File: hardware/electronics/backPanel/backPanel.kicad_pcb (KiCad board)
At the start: 2 copper layers, 104 x 54.6 mm, 8 parts, among them J1 Untitled, J2 Untitled, J3 Untitled, J4 7793, J5 M3, J6 M3, J7 M3, J8 M3

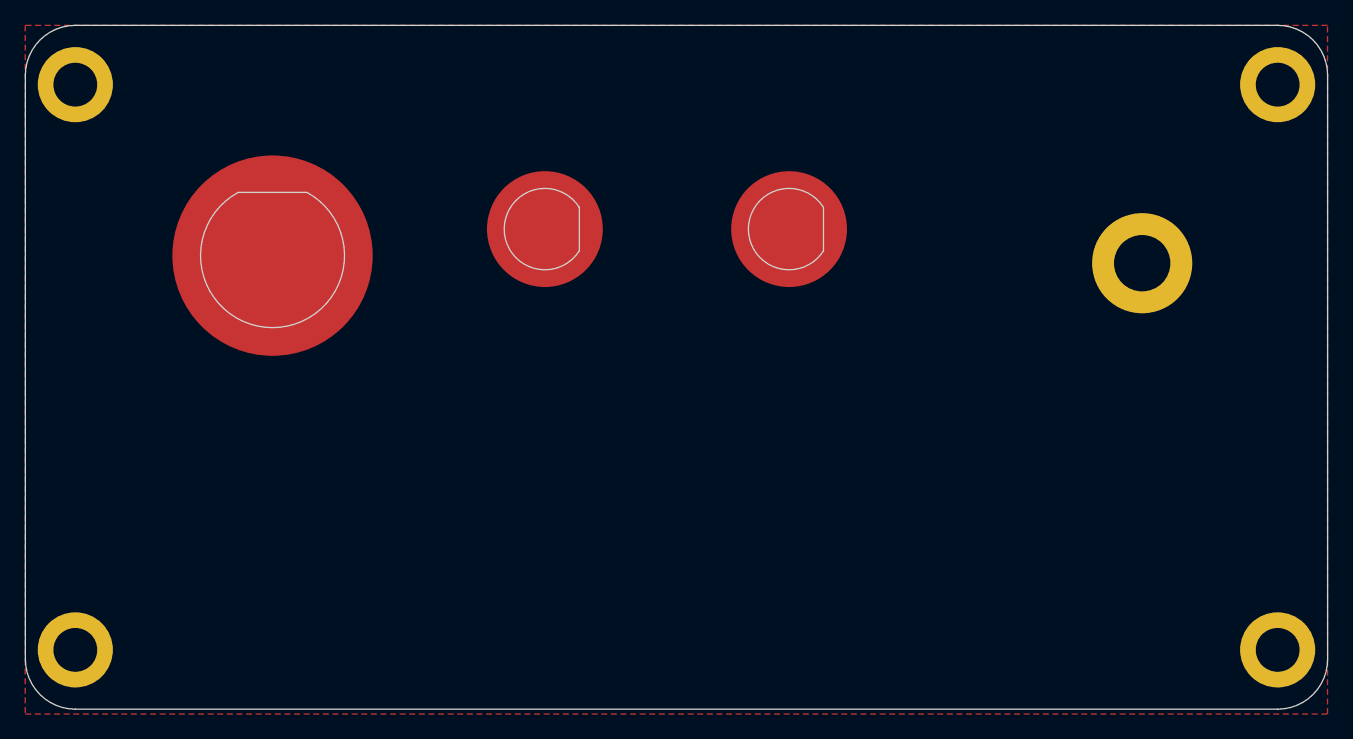
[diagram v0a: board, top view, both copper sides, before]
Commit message: front/back enclosure panels
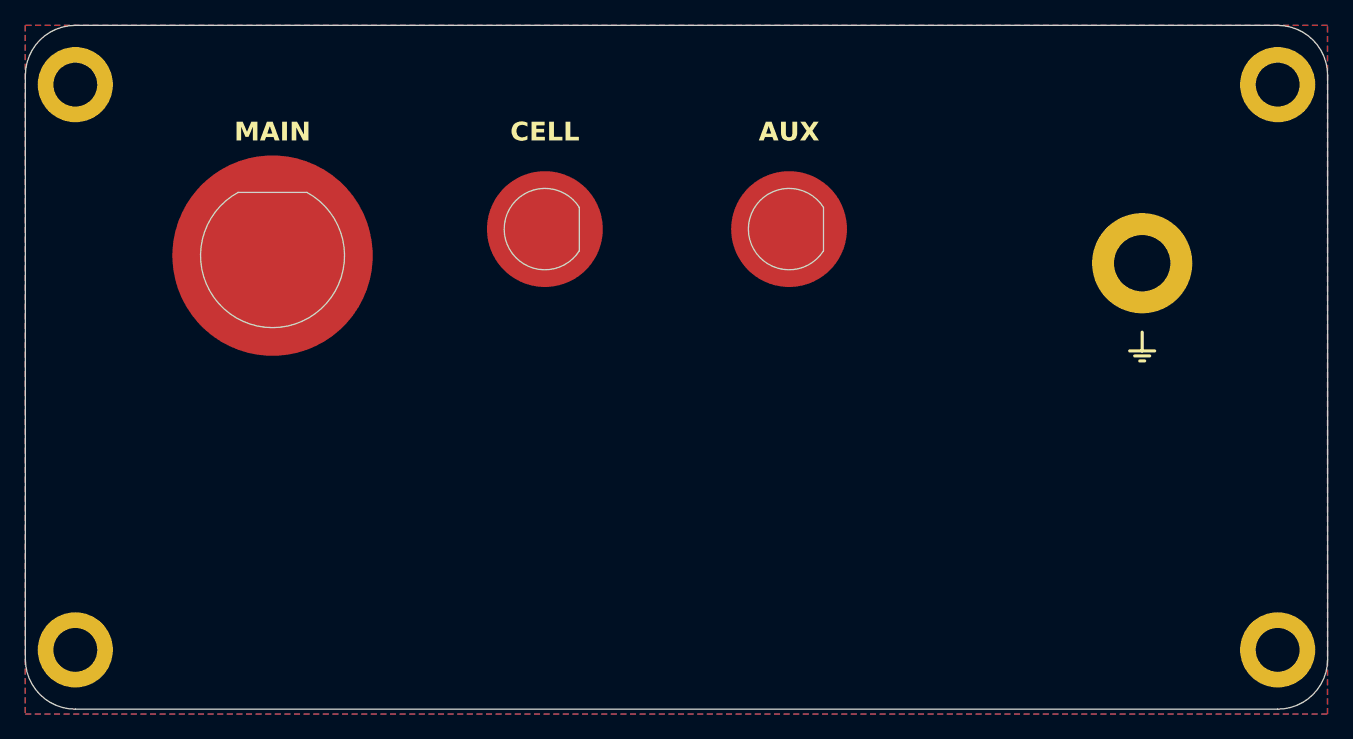
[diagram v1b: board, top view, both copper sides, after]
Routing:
- added copper zone on B.Cu, net GND
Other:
- board text added: "AUX"
- board text added: "CELL"
- board text added: "MAIN"
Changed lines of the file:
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@@
 		(embedded_fonts no)
+	)
+	(gr_line
+		(start 179 106.8)
+		(end 179.4 106.8)
+		(stroke
+			(width 0.25)
+			(type solid)
+		)
+		(layer "F.SilkS")
+	)
+	(gr_line
+		(start 178.6 106.4)
+		(end 179.8 106.4)
+		(stroke
+			(width 0.25)
+			(type solid)
+		)
+		(layer "F.SilkS")
+	)
+	(gr_line
+		(start 179.2 104.5)
+		(end 179.2 106)
+		(stroke
+			(width 0.25)
+			(type solid)
+		)
+		(layer "F.SilkS")
+	)
+	(gr_line
+		(start 178.2 106)
+		(end 180.2 106)
+		(stroke
+			(width 0.25)
+			(type solid)
+		)
+		(layer "F.SilkS")
 	)
 	(gr_arc
@@
 		)
 		(layer "Edge.Cuts")
+	)
+	(gr_text "AUX"
+		(at 151 88.5 0)
+		(layer "F.SilkS")
+		(effects
+			(font
+				(face "Arial")
+				(size 1.5 1.5)
+				(thickness 0.3)
+				(bold yes)
+			)
+		)
+		(render_cache "AUX" 0
+			(polygon
+				(pts
+					(xy 150.292276 89.1225) (xy 149.962273 89.1225) (xy 149.831115 88.782513) (xy 149.230735 88.782513)
+					(xy 149.106721 89.1225) (xy 148.784962 89.1225) (xy 149.014897 88.530455) (xy 149.323975 88.530455)
+					(xy 149.733845 88.530455) (xy 149.526849 87.967719) (xy 149.323975 88.530455) (xy 149.014897 88.530455)
+					(xy 149.370045 87.61601) (xy 149.690797 87.61601)
+				)
+			)
+			(polygon
+				(pts
+					(xy 150.450911 87.61601) (xy 150.754169 87.61601) (xy 150.754169 88.439322) (xy 150.757853 88.618371)
+					(xy 150.765435 88.693395) (xy 150.78465 88.752054) (xy 150.815323 88.8015) (xy 150.858125 88.843238)
+					(xy 150.909884 88.873342) (xy 150.975473 88.892706) (xy 151.058527 88.89975) (xy 151.143145 88.892843)
+					(xy 151.206385 88.874333) (xy 151.253158 88.846352) (xy 151.291596 88.807367) (xy 151.317496 88.764002)
+					(xy 151.332018 88.715194) (xy 151.341336 88.624569) (xy 151.34539 88.456999) (xy 151.34539 87.61601)
+					(xy 151.648739 87.61601) (xy 151.648739 88.409188) (xy 151.6412 88.661199) (xy 151.624101 88.793413)
+					(xy 151.602544 88.865826) (xy 151.57227 88.928557) (xy 151.533426 88.982915) (xy 151.485805 89.029773)
+					(xy 151.427398 89.070827) (xy 151.356655 89.106013) (xy 151.281421 89.130039) (xy 151.186481 89.145966)
+					(xy 151.067777 89.151809) (xy 150.923632 89.145067) (xy 150.81753 89.127375) (xy 150.741347 89.101892)
+					(xy 150.670502 89.064018) (xy 150.612479 89.020745) (xy 150.565675 88.972107) (xy 150.51142 88.888938)
+					(xy 150.480587 88.804678) (xy 150.459594 88.659457) (xy 150.450911 88.421461)
+				)
+			)
+			(polygon
+				(pts
+					(xy 151.815527 89.1225) (xy 152.335214 88.338846) (xy 151.863704 87.61601) (xy 152.218253 87.61601)
+					(xy 152.515649 88.066821) (xy 152.814602 87.61601) (xy 153.166037 87.61601) (xy 152.693885 88.336923)
+					(xy 153.212199 89.1225) (xy 152.846384 89.1225) (xy 152.513542 88.612246) (xy 152.179326 89.1225)
+				)
+			)
+		)
+	)
+	(gr_text "CELL"
+		(at 131.5 88.5 0)
+		(layer "F.SilkS")
+		(effects
+			(font
+				(face "Arial")
+				(size 1.5 1.5)
+				(thickness 0.3)
+				(bold yes)
+			)
+		)
+		(render_cache "CELL" 0
+			(polygon
+				(pts
+					(xy 129.874166 88.565626) (xy 130.168265 88.659415) (xy 130.126303 88.780938) (xy 130.074475 88.880565)
+					(xy 130.013496 88.961486) (xy 129.943318 89.026146) (xy 129.862223 89.077128) (xy 129.77004 89.114436)
+					(xy 129.66484 89.137768) (xy 129.544255 89.145947) (xy 129.425899 89.137333) (xy 129.319213 89.11237)
+					(xy 129.222314 89.071717) (xy 129.133699 89.015137) (xy 129.05232 88.941516) (xy 128.985229 88.85714)
+					(xy 128.932168 88.760992) (xy 128.89299 88.651371) (xy 128.868356 88.526083) (xy 128.859704 88.382535)
+					(xy 128.868561 88.229799) (xy 128.893638 88.097936) (xy 128.933248 87.983969) (xy 128.986496 87.88536)
+					(xy 129.053327 87.800108) (xy 129.13497 87.72594) (xy 129.225262 87.668592) (xy 129.325419 87.627108)
+					(xy 129.43717 87.601463) (xy 129.562665 87.592562) (xy 129.698743 87.603536) (xy 129.816755 87.634897)
+					(xy 129.919864 87.685437) (xy 130.010454 87.755503) (xy 130.07043 87.825247) (xy 130.121927 87.916044)
+					(xy 130.164144 88.032199) (xy 129.863908 88.102541) (xy 129.839054 88.028735) (xy 129.802082 87.967975)
+					(xy 129.752717 87.918169) (xy 129.693242 87.880999) (xy 129.625488 87.85835) (xy 129.547278 87.850483)
+					(xy 129.466077 87.858322) (xy 129.395094 87.880938) (xy 129.332253 87.918036) (xy 129.276168 87.970742)
+					(xy 129.234517 88.032613) (xy 129.202001 88.114586) (xy 129.180272 88.221698) (xy 129.172213 88.360004)
+					(xy 129.180333 88.507757) (xy 129.20204 88.620308) (xy 129.234143 88.704703) (xy 129.274703 88.766851)
+					(xy 129.330121 88.820121) (xy 129.391989 88.857473) (xy 129.461648 88.880173) (xy 129.541141 88.888026)
+					(xy 129.618776 88.879198) (xy 129.687386 88.853432) (xy 129.749145 88.810266) (xy 129.798761 88.752992)
+					(xy 129.840843 88.673372)
+				)
+			)
+			(polygon
+				(pts
+					(xy 130.428292 89.1225) (xy 130.428292 87.61601) (xy 131.542131 87.61601) (xy 131.542131 87.868068)
+					(xy 130.73155 87.868068) (xy 130.73155 88.202192) (xy 131.485711 88.202192) (xy 131.485711 88.454251)
+					(xy 130.73155 88.454251) (xy 130.73155 88.870441) (xy 131.570799 88.870441) (xy 131.570799 89.1225)
+				)
+			)
+			(polygon
+				(pts
+					(xy 131.835956 89.1225) (xy 131.835956 87.633595) (xy 132.139305 87.633595) (xy 132.139305 88.870441)
+					(xy 132.893466 88.870441) (xy 132.893466 89.1225)
+				)
+			)
+			(polygon
+				(pts
+					(xy 133.118231 89.1225) (xy 133.118231 87.633595) (xy 133.42158 87.633595) (xy 133.42158 88.870441)
+					(xy 134.175741 88.870441) (xy 134.175741 89.1225)
+				)
+			)
+		)
+	)
+	(gr_text "MAIN"
+		(at 109.75 88.5 0)
+		(layer "F.SilkS")
+		(effects
+			(font
+				(face "Arial")
+				(size 1.5 1.5)
+				(thickness 0.3)
+				(bold yes)
+			)
+		)
+		(render_cache "MAIN" 0
+			(polygon
+				(pts
+					(xy 107.217507 89.1225) (xy 107.217507 87.61601) (xy 107.671433 87.61601) (xy 107.944008 88.643661)
+					(xy 108.213468 87.61601) (xy 108.668493 87.61601) (xy 108.668493 89.1225) (xy 108.386667 89.1225)
+					(xy 108.386667 87.93667) (xy 108.088538 89.1225) (xy 107.796454 89.1225) (xy 107.499333 87.93667)
+					(xy 107.499333 89.1225)
+				)
+			)
+			(polygon
+				(pts
+					(xy 110.324551 89.1225) (xy 109.994548 89.1225) (xy 109.86339 88.782513) (xy 109.263011 88.782513)
+					(xy 109.138996 89.1225) (xy 108.817237 89.1225) (xy 109.047173 88.530455) (xy 109.35625 88.530455)
+					(xy 109.76612 88.530455) (xy 109.559124 87.967719) (xy 109.35625 88.530455) (xy 109.047173 88.530455)
+					(xy 109.402321 87.61601) (xy 109.723072 87.61601)
+				)
+			)
+			(polygon
+				(pts
+					(xy 110.475951 89.1225) (xy 110.475951 87.61601) (xy 110.779301 87.61601) (xy 110.779301 89.1225)
+				)
+			)
+			(polygon
+				(pts
+					(xy 111.071568 89.1225) (xy 111.071568 87.61601) (xy 111.366674 87.61601) (xy 111.981433 88.624519)
+					(xy 111.981433 87.61601) (xy 112.263259 87.61601) (xy 112.263259 89.1225) (xy 111.958902 89.1225)
+					(xy 111.353302 88.129011) (xy 111.353302 89.1225)
+				)
+			)
+		)
 	)
 	(zone
@@
 		(net_name "GND")
 		(locked yes)
-		(layer "F.Cu")
+		(layers "F.Cu" "B.Cu")
 		(hatch edge 0.5)
 		(connect_pads yes
